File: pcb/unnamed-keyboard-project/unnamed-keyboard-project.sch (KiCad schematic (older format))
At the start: 1 part

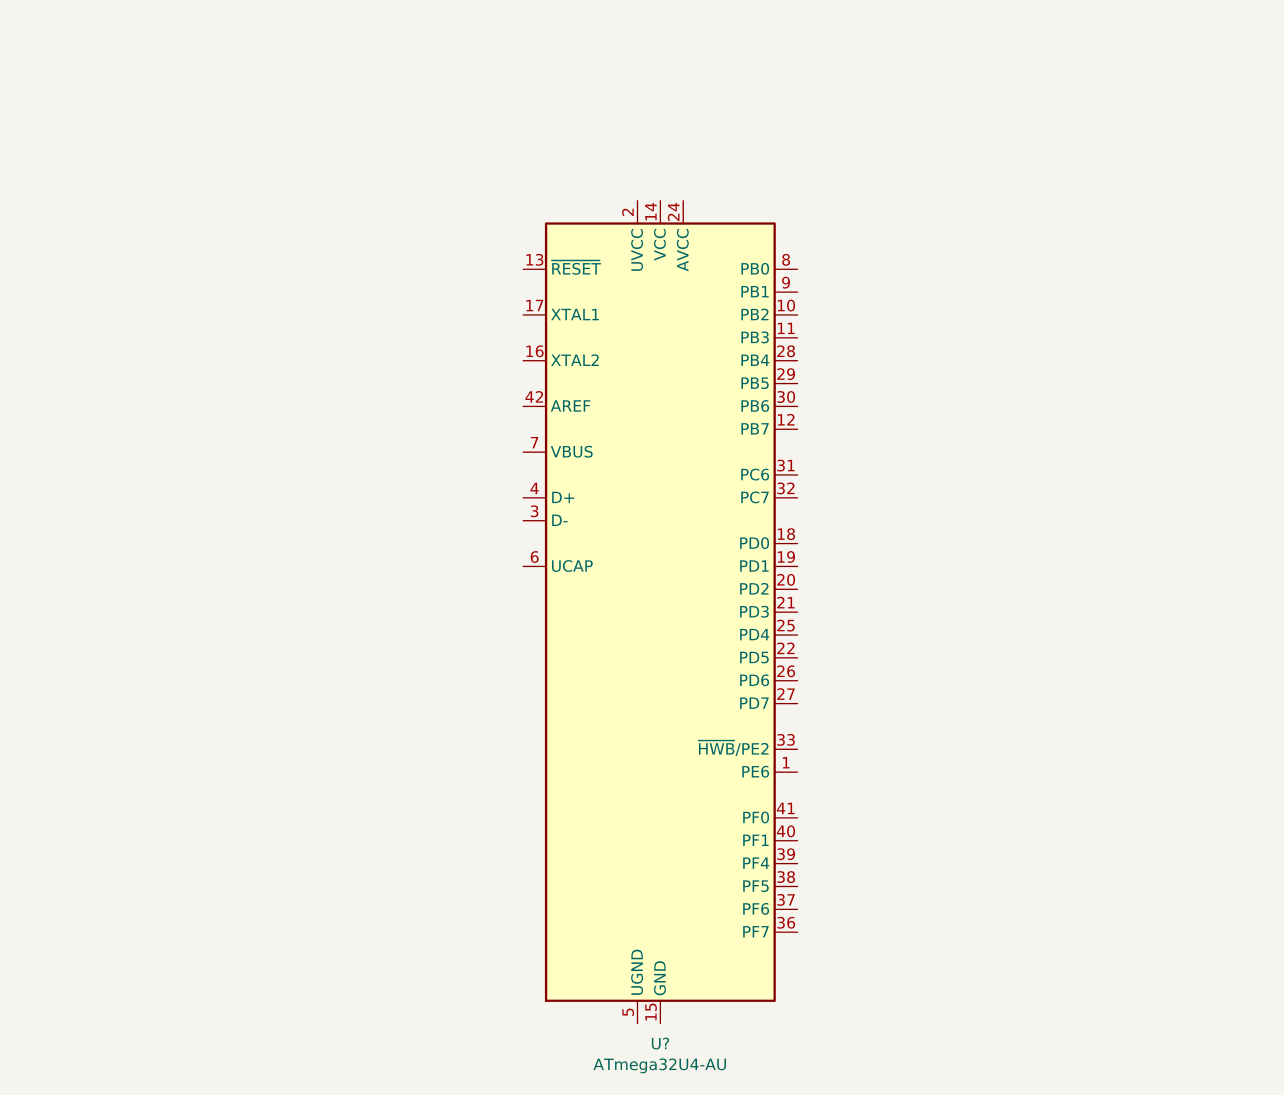
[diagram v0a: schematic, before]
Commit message: Update 12/11/19 23:46
Added microprocessor and peripherals to schematic. Added empty BOM excel sheet.
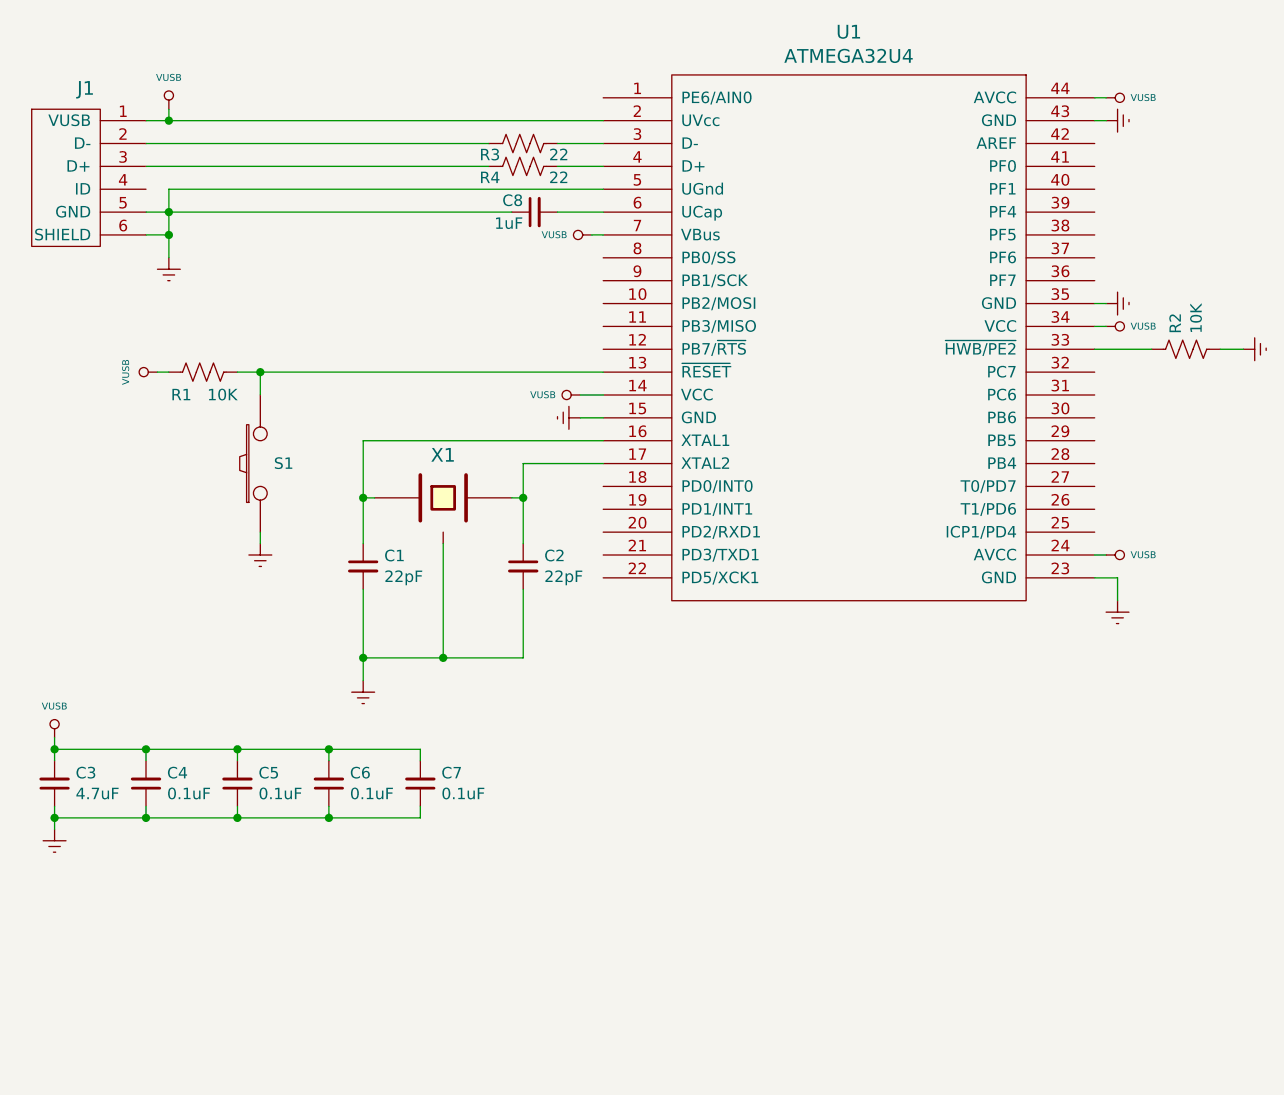
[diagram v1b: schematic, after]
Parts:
- removed U?: ATmega32U4-AU, Package_QFP:TQFP-44_10x10mm_P0.8mm, symbol MCU_Microchip_ATmega:ATmega32U4-AU
- added C1, C2: 22pF, symbol Device:C_Small
- added C3: 4.7uF, symbol Device:C_Small
- added C4, C5, C6, C7: 0.1uF, symbol Device:C_Small
- added C8: 1uF, symbol Device:C_Small
- added J1: USB_mini_micro_B, symbol keyboard_parts:USB_mini_micro_B
- added R1, R2: 10K, symbol Device:R_US
- added R3, R4: 22, symbol Device:R_US
- added S1: SW_PUSH, symbol keyboard_parts:SW_PUSH
- added U1: ATMEGA32U4, symbol keyboard_parts:ATMEGA32U4
- added X1: XTAL_GND, symbol keyboard_parts:XTAL_GND
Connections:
- new net: R1.1, S1.2, U1.13 (~RESET)
- new net: C1.1, U1.16 (XTAL1), X1.1
- new net: C2.1, U1.17 (XTAL2), X1.2
- new net: R3.1, U1.3 (D-)
- new net: R2.2, U1.33 (~HWB/PE2)
- new net: R4.1, U1.4 (D+)
- new net: C8.2, U1.6 (UCap)
- new net: J1.2 (D-), R3.2
- new net: J1.3 (D+), R4.2
- new net GNDREF: C1.2, C2.2, C3.1, C4.1, C5.1, C6.1, C7.1, C8.1, J1.5 (GND), J1.6 (SHIELD), R2.1, S1.1, U1.15 (GND), U1.23 (GND), U1.35 (GND), U1.43 (GND), U1.5 (UGnd), X1.3
- new net VUSB: C3.2, C4.2, C5.2, C6.2, C7.2, J1.1 (VUSB), R1.2, U1.14 (VCC), U1.2 (UVcc), U1.24 (AVCC), U1.34 (VCC), U1.44 (AVCC), U1.7 (VBus)
